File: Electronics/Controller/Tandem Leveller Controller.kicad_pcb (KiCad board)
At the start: 2 copper layers, 212 x 145 mm, 137 parts, among them J1 Conn_01x02, J10 CAN BUS, J11 TRACTOR BATTERY, J12 PWR SWITCH, J13 VALVE POWER, J14 TABLET 1 PWR, J15 TABLET 2 PWR, J16 SLAVE TABLET, J17 MASTER TABLET, J18 292303-7, J19 292303-7, J2 GPS SIM, J20 FRONT HEIGHT, J21 REAR HEIGHT, J22 SWITCHES, J23 CAN, J3 Conn_01x02, J4 Conn_01x02, J5 Conn_01x02, J6 Conn_01x02, J7 Conn_01x02, J8 Conn_01x02, J9 TERM, U1 TEENSY 4.0, U10 FT232RL, U11 FT232RL, U12 FT232RL, U13 FT232RL, U14 FT232RL, U15 FT232RL, U16 USB2517, U17 MIC2026-1YM, U2 simpleRTK2B, U3 simpleRTK2B, U4 simpleRTK2B, U5 TJA1462ATK-0Z, U6 PESD2CANFD24V-TR, U7 LM2596S-5, U8 LM2587S-ADJ/NOPB, U9 LM2587S-ADJ/NOPB, Y1 FA-238 24.0000MD30X-W5

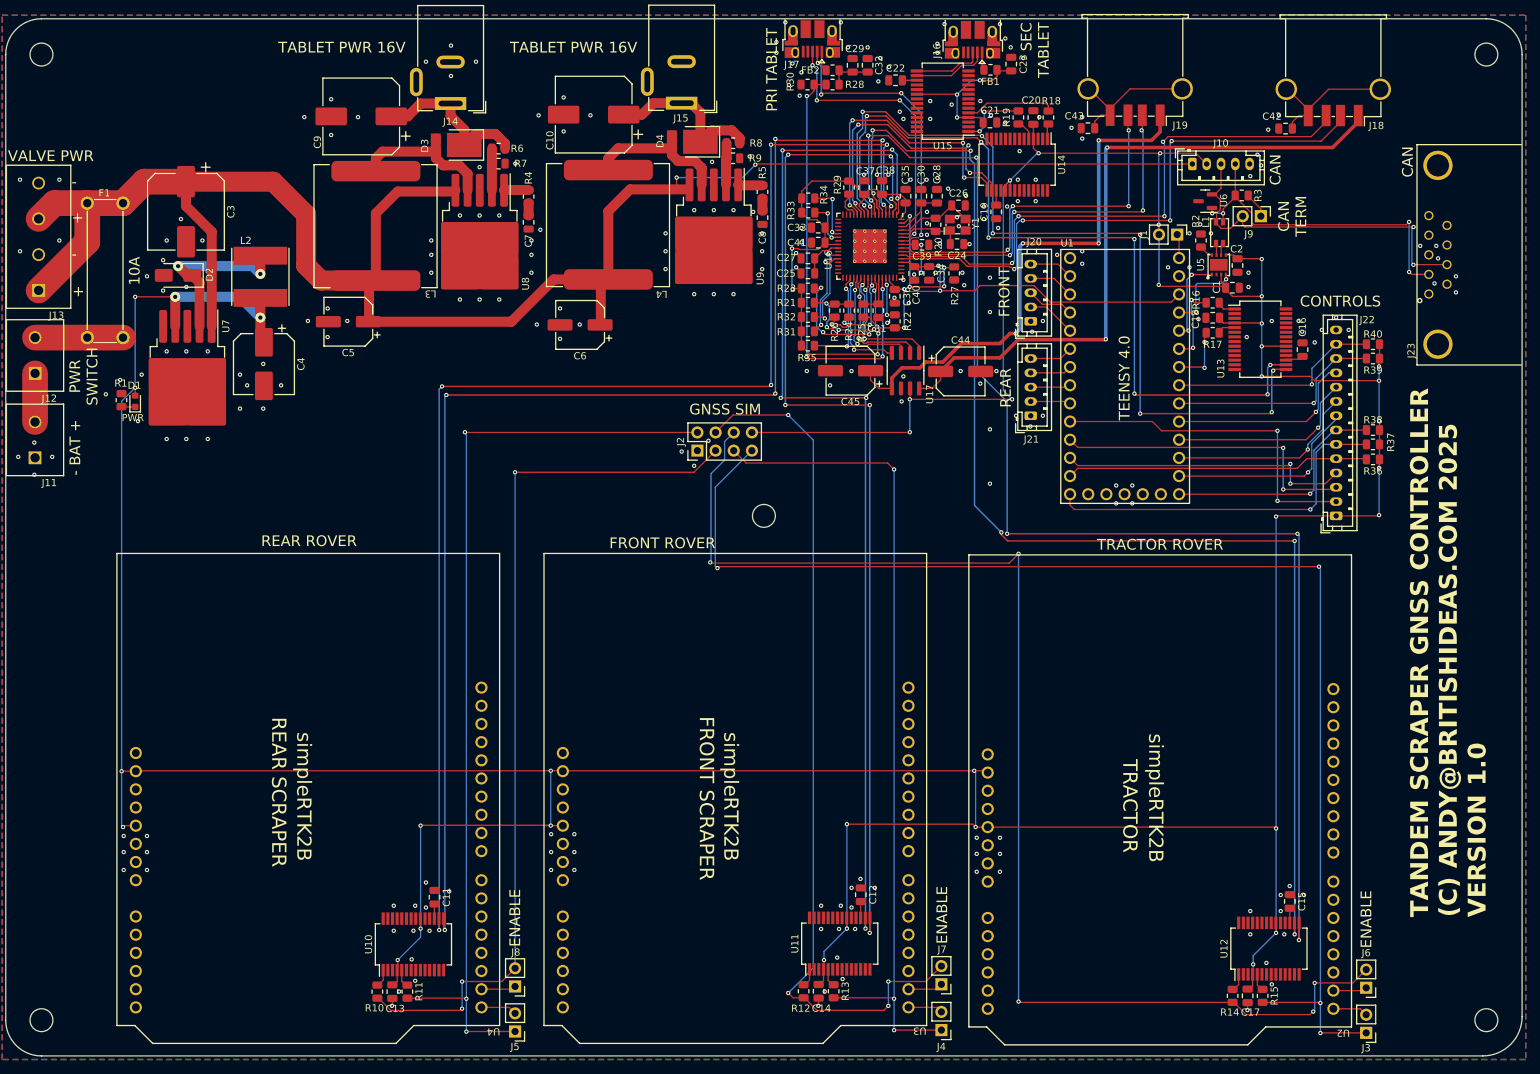
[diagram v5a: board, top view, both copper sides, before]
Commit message: Moved controls from GPIO to CAN bus. Added two more CAN bus connectors. Changed GNSS SIM connector from pin header to JST-PH.
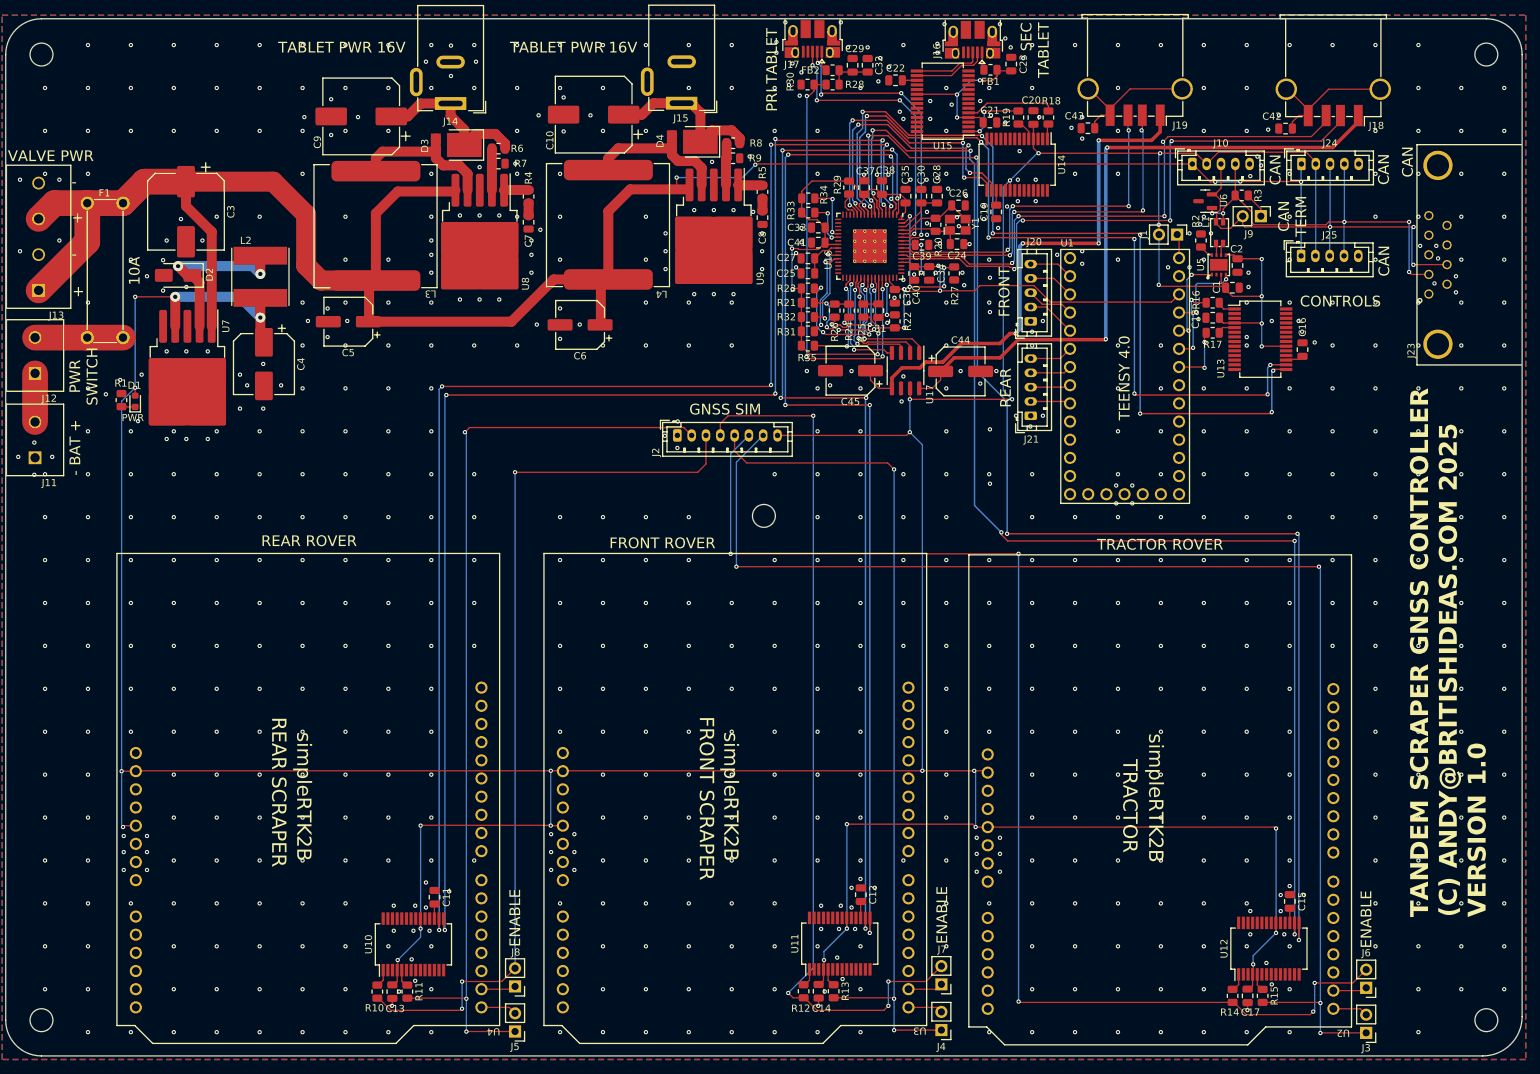
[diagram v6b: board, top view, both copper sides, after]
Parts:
- removed J22: SWITCHES, Connector_JST:JST_PH_B14B-PH-K_1x14_P2.00mm_Vertical
- removed R36, R37, R38, R39, R40: 10k, Resistor_SMD:R_0805_2012Metric
- added J24: CAN BUS, Connector_JST:JST_PH_B5B-PH-K_1x05_P2.00mm_Vertical, F.Cu at (235.2, 44.3)
- added J25: CAN BUS, Connector_JST:JST_PH_B5B-PH-K_1x05_P2.00mm_Vertical, F.Cu at (235.1, 57.1)
- J2: footprint Connector_PinHeader_2.54mm:PinHeader_2x04_P2.54mm_Vertical -> Connector_JST:JST_PH_B8B-PH-K_1x08_P2.00mm_Vertical
- moved J2 3.52 mm to (147.9, 82.2), turned to 0 degrees
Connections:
- net /IMU and Sensors/CAN_H renamed /CAN/CAN_H
- net /IMU and Sensors/CAN_L renamed /CAN/CAN_L
- net /IMU and Sensors/CAN_RX renamed /CAN/CAN_RX
- net /IMU and Sensors/CAN_TX renamed /CAN/CAN_TX
- U1 pad 10: /~{AUTO_HEIGHT_ON} -> unconnected-(U1-GPIO8_TX2-Pad10)
- U1 pad 11: /User Controls/STATUS_LAMP_1 -> unconnected-(U1-GPIO9-Pad11)
- U1 pad 12: /User Controls/STATUS_LAMP_2 -> unconnected-(U1-GPIO10_CS-Pad12)
- U1 pad 13: /User Controls/WORK_BUTTON -> unconnected-(U1-GPIO11_MOSI-Pad13)
- U1 pad 14: /User Controls/JOYSTICK1_SEL -> unconnected-(U1-GPIO12_MISO-Pad14)
- U1 pad 20: /User Controls/JOYSTICK2_SEL -> unconnected-(U1-GPIO13_SCK_CRX1-Pad20)
- U1 pad 21: /User Controls/JOYSTICK1_VERT -> unconnected-(U1-GPIO14_TX3-Pad21)
- U1 pad 22: /User Controls/JOYSTICK1_HORI -> unconnected-(U1-GPIO15_RX3-Pad22)
- U1 pad 23: /User Controls/JOYSTICK2_VERT -> unconnected-(U1-GPIO16_RX4_SCL1-Pad23)
- U1 pad 24: /User Controls/JOYSTICK2_HORI -> unconnected-(U1-GPIO17_TX4_SDA1-Pad24)
- U1 pad 25: /User Controls/MISC_BUTTON_1 -> unconnected-(U1-GPIO18_SDA0-Pad25)
- U1 pad 26: /User Controls/MISC_BUTTON_2 -> unconnected-(U1-GPIO19_SCL0-Pad26)
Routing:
- net /User Controls/JOYSTICK1_SEL: track 51.2 -> 0.00 mm, vias 1 -> 0
- net /~{AUTO_HEIGHT_ON}: track 47.6 -> 0.00 mm, vias 2 -> 0
- net /User Controls/STATUS_LAMP_1: track 43.6 -> 0.00 mm, vias 2 -> 0
- net /User Controls/WORK_BUTTON: track 42.5 -> 0.00 mm
- net /User Controls/STATUS_LAMP_2: track 41.1 -> 0.00 mm, vias 2 -> 0
- net /User Controls/JOYSTICK2_SEL: track 33.2 -> 0.00 mm, vias 1 -> 0
- net /User Controls/MISC_BUTTON_1: track 30.6 -> 0.00 mm, vias 1 -> 0
- net /User Controls/MISC_BUTTON_2: track 29.9 -> 0.00 mm, vias 1 -> 0
- net +12V: track 262.9 -> 292.1 mm, vias 2 -> 5
- net +5V: track 676.4 -> 647.8 mm, vias 38 -> 32
- net /User Controls/JOYSTICK1_VERT: track 27.8 -> 0.00 mm, vias 1 -> 0
- net /User Controls/JOYSTICK2_HORI: track 26.9 -> 0.00 mm, vias 1 -> 0
- net /User Controls/JOYSTICK2_VERT: track 26.9 -> 0.00 mm, vias 1 -> 0
- net /User Controls/JOYSTICK1_HORI: track 26.8 -> 0.00 mm, vias 1 -> 0
- net /CAN/CAN_L: track 48.0 -> 60.9 mm, vias 4 -> 5
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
